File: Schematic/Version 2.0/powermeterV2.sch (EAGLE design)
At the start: 75 parts, among them K2 RT314F03, Q1 S8050, Q2 S8050, Q3 S8050, Q4 S8050, Y1 16MHz, Y2 NX2012SA-32.768K-STD-MUB-1

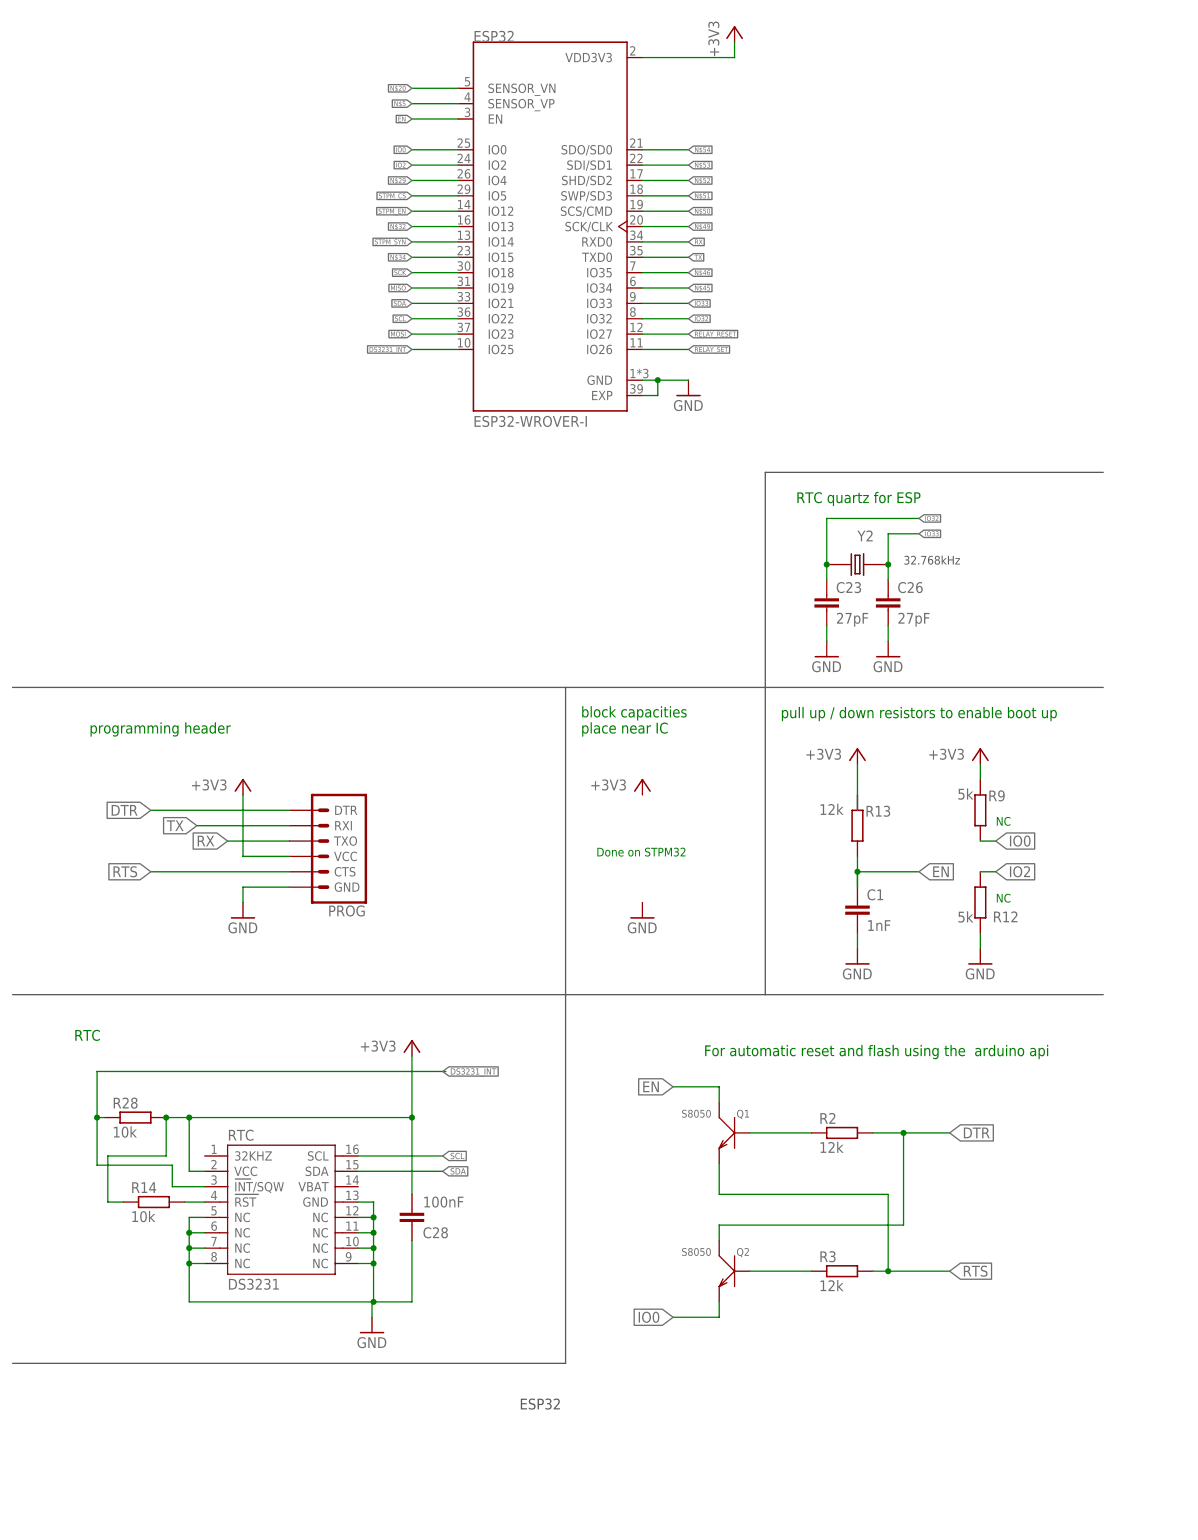
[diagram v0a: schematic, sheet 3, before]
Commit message: new firmware with RTC support, PSRAM, new schematic/board with error LED, I2C pullups etc, diodes
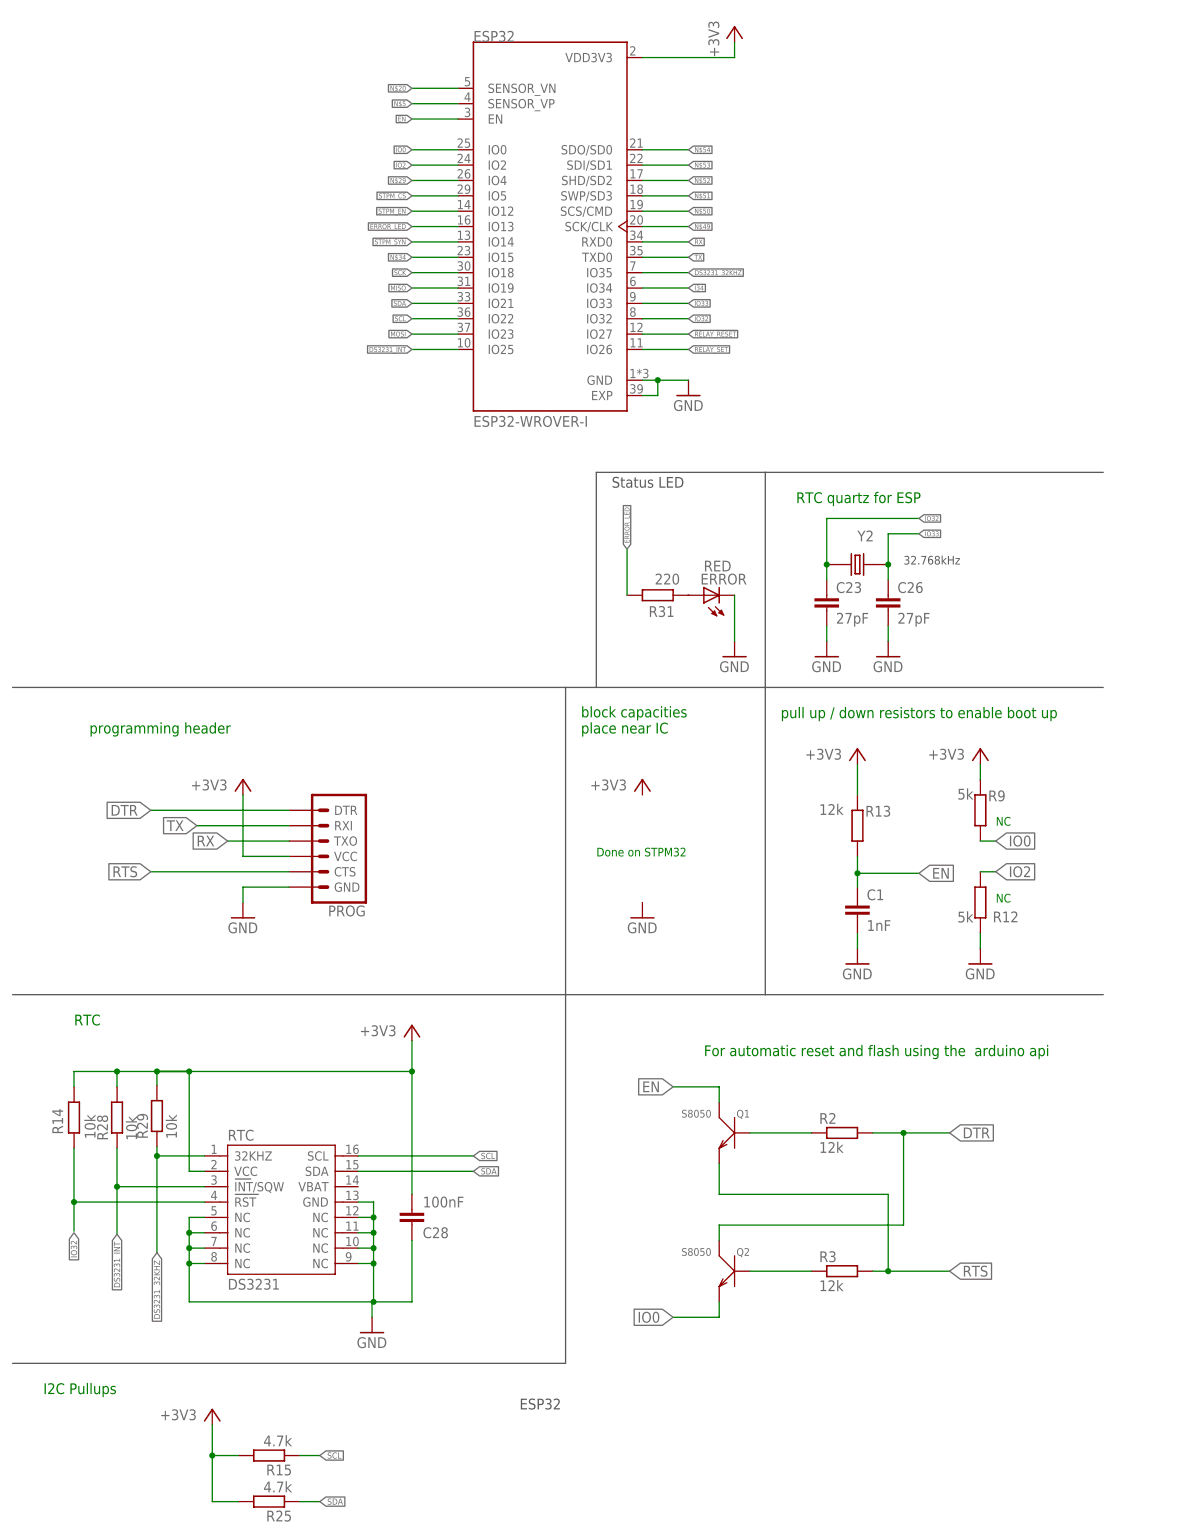
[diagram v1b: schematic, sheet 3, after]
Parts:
- removed K2: RT314F03, RT314F03:RT314F03
- added D1, D2: 1N4148, Seeed-OPL-Diode:SMD-DIODE-SWITCH-1N4148(LL-34)
- added ERROR: RED, led:LEDCHIP-LED0805
- added R15: 4.7k, resistor:R-EU_R0603
- added R29: 10k, resistor:R-EU_R0603
- added R31: 220, resistor:R-EU_R0603
- added RELAY: RT314F03, RT314F03:RT314F03
- R14, R28: device resistor:R-EU_R0402 -> resistor:R-EU_R0603
- R25: value 220 -> 4.7k; device resistor:R-EU_R0402 -> resistor:R-EU_R0603
- R26, R27: value 10k -> 1.8k
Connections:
- net N$45 renamed I34
- removed net N$18: K2.A3, R25.1
- removed net N$26: R14.2, RTC.RST
- removed net N$32: ESP32.IO13
- removed net N$46: ESP32.IO35
- new net DS3231_32KHZ: ESP32.IO35, R29.1, RTC.32KHZ
- new net ERROR_LED: ESP32.IO13, R31.1
- new net N$16: ERROR.A, R31.2
- net +3V3: now also D1.-, D2.-, R15.2, R29.2, RELAY.A3
- net AC_N_SHUNT: now also RELAY.11; no longer K2.11
- net GND: now also ERROR.C
- net IO32: now also R14.2, RTC.RST
- net N$17: now also D1.+, RELAY.A1; no longer K2.A1
- net N$28: now also D2.+, RELAY.A2; no longer K2.A2
- net N$4: now also RELAY.14; no longer K2.14
- net SCL: now also R15.1
- net SDA: now also R25.1
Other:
- note added: "I2C Pullups"
- note added: "Status LED"
- note added: "bistable relay"
- note removed: "Used pullup and pulldown for default state not working with 10k, working with 220 NOTE: try with 1k, Replace 220 with sth else, diode?"
- note removed: "solid state relay"
- moved on the sheet: R14, R28

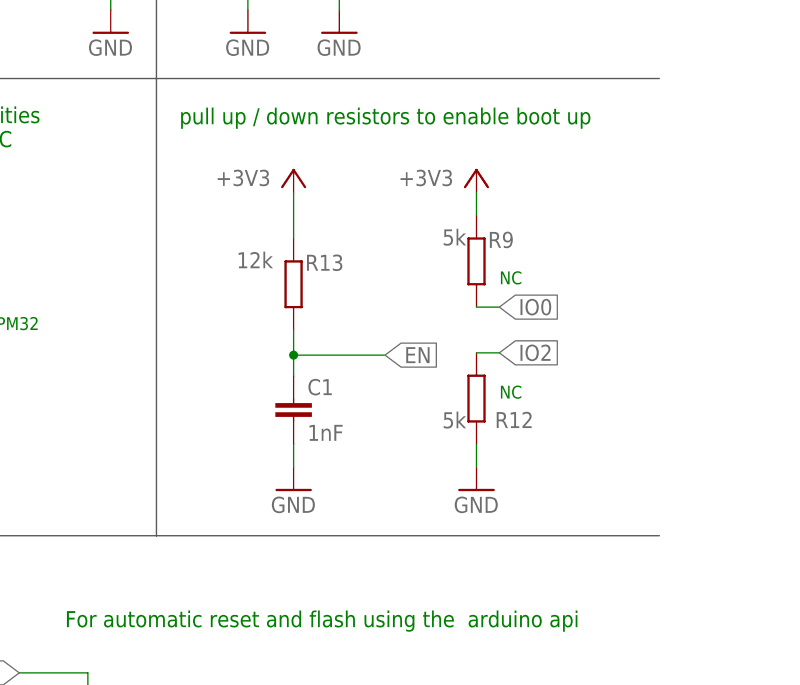
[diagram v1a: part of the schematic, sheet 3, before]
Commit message: fixed board/schematic inconsistencies. added 100nF on IO0
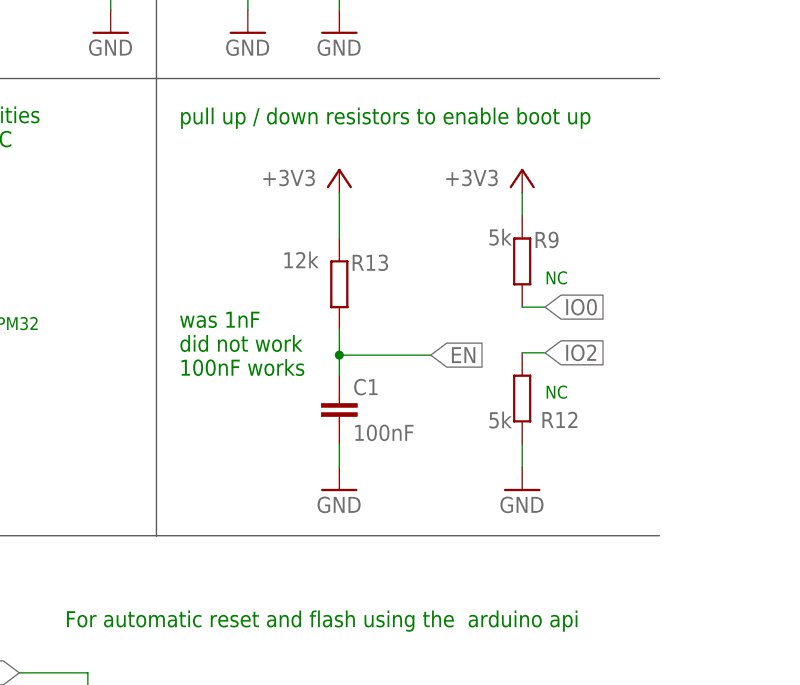
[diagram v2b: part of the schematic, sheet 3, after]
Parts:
- C1: value 1nF -> 100nF
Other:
- note added: "was 1nF did not work 100nF works"
- moved on the sheet: C1, R12, R13, R9
